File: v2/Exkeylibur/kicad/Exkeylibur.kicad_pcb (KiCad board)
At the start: 2 copper layers, 131.1 x 95.8 mm, 25 parts, among them SW1 SW_Push, SW10 SW_Push, SW11 SW_Push, SW12 SW_Push, SW13 SW_Push, SW14 SW_Push, SW15 SW_Push, SW16 SW_Push, SW17 SW_Push, SW18 SW_Push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

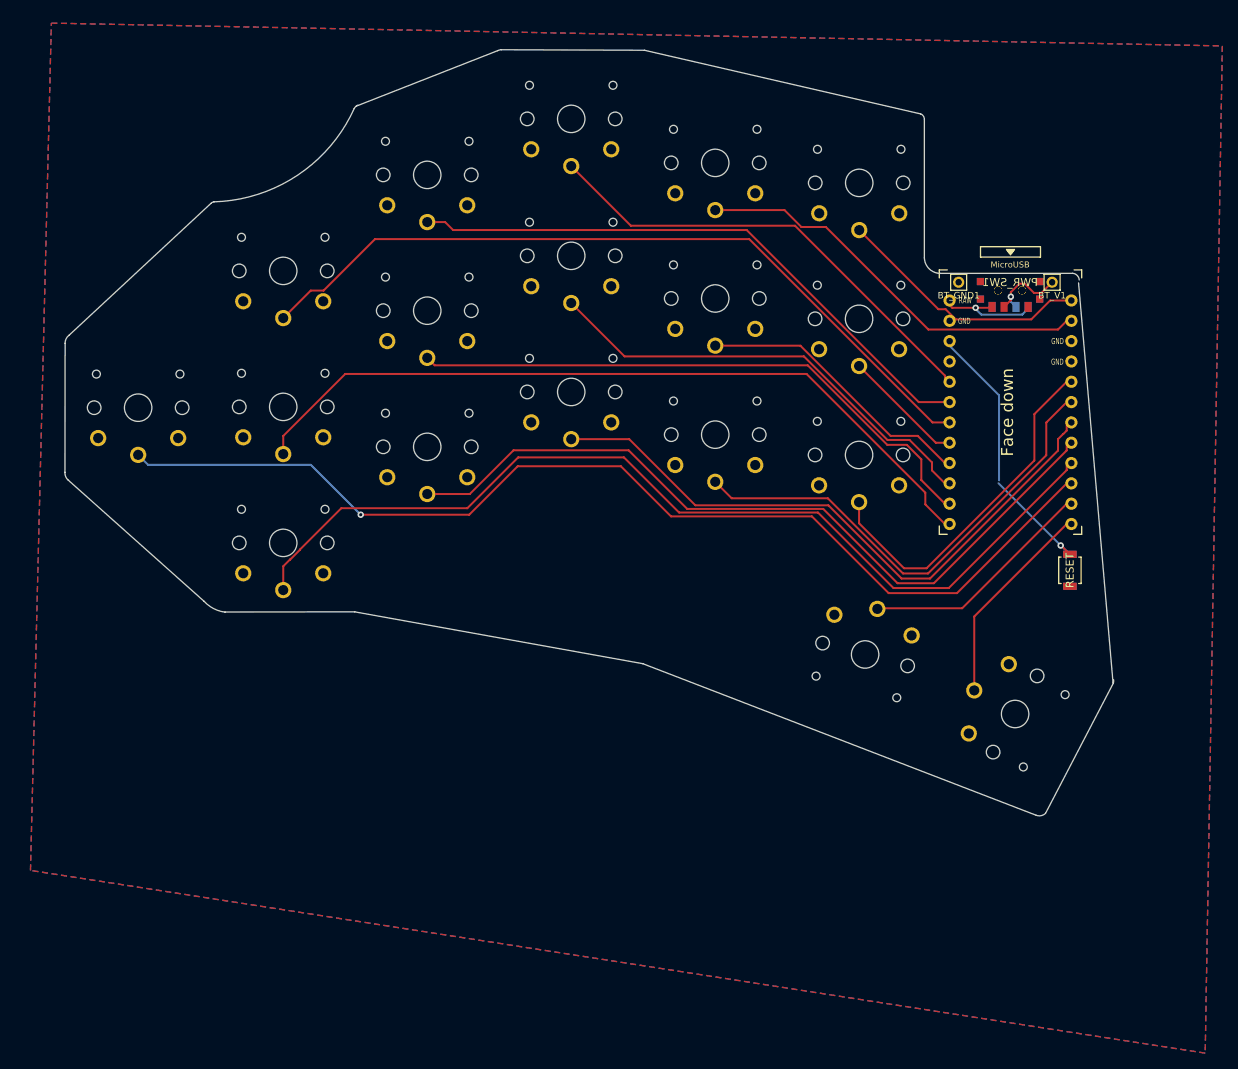
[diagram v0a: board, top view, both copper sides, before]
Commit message: add more room for the 1.5u keycap
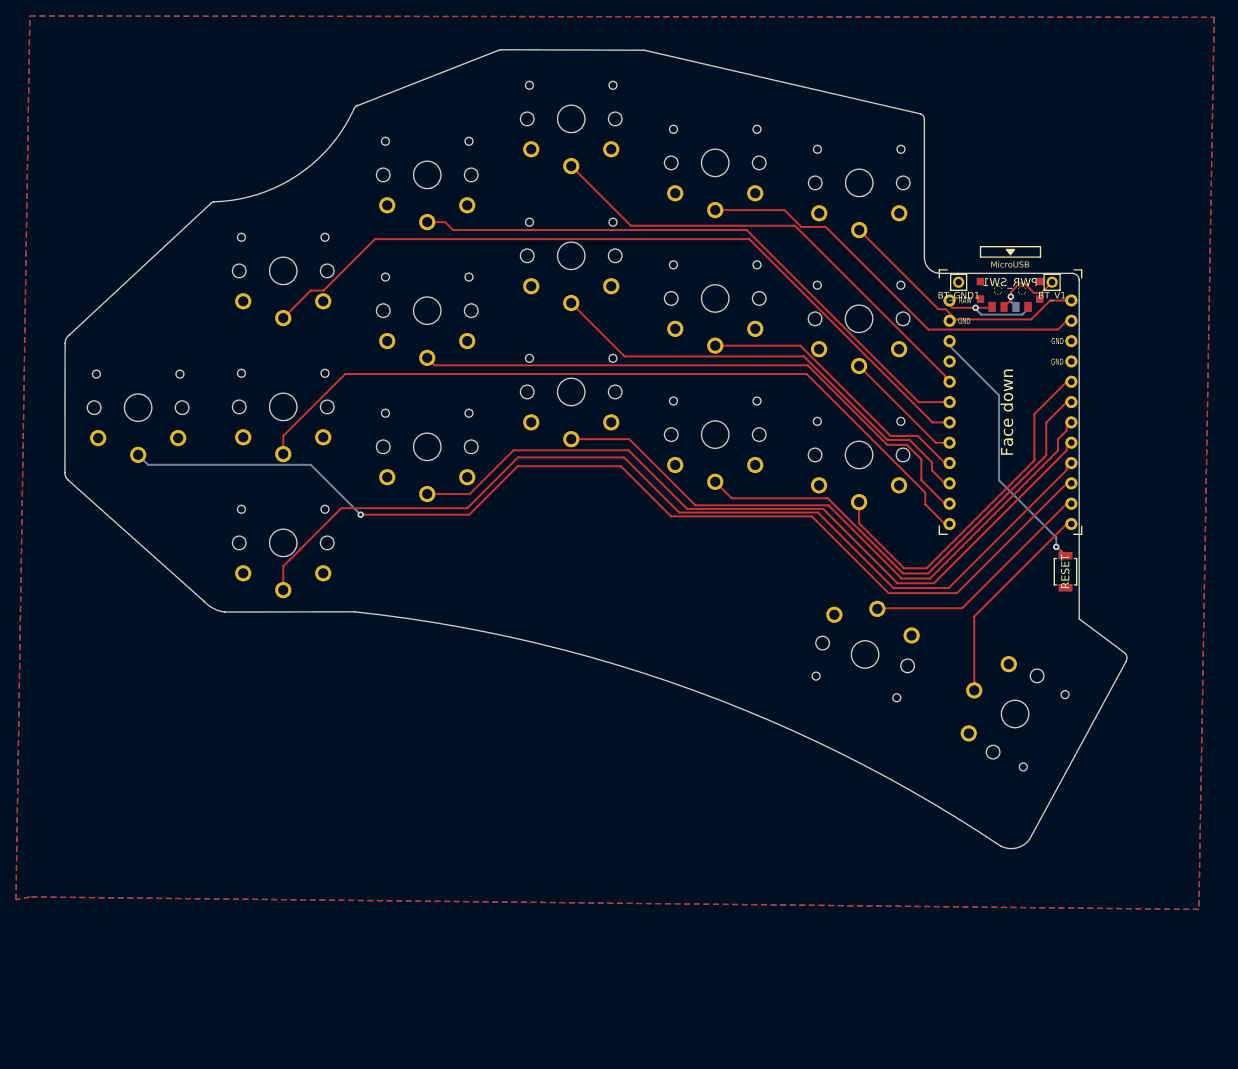
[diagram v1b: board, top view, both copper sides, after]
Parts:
- moved RSW1 0.58 mm to (145.6, 86.6) (x2)
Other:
- board size 131.1 x 95.8 mm -> 132.8 x 99.9 mm
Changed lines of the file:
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@@
   )
   (footprint "Exkeylibur:reset_switch" (layer "F.Cu")
-    (at 146.130425 86.446425 -90)
+    (at 145.57885 86.619158 -90)
     (descr "Ultra-small-sized Tactile Switch with High Contact Reliability, Top-actuated Model, without Ground Terminal, without Boss")
     (tags "Tactile Switch")
@@
   )
   (footprint "Exkeylibur:reset_switch" (layer "B.Cu")
-    (at 146.132 86.453692 -90)
+    (at 145.580425 86.626425 -90)
     (descr "Ultra-small-sized Tactile Switch with High Contact Reliability, Top-actuated Model, without Ground Terminal, without Boss")
     (tags "Tactile Switch")
@@
   (gr_arc (start 127.471526 29.394101) (mid 127.809899 29.662221) (end 127.93758 30.074631) (layer "Edge.Cuts") (width 0.05))
   (gr_line (start 129.972537 49.330129) (end 146.48327 49.322) (layer "Edge.Cuts") (width 0.05))
-  (gr_line (start 147.210425 50.516425) (end 151.520425 100.506425) (layer "Edge.Cuts") (width 0.05))
+  (gr_line (start 147.290425 50.156425) (end 147.290425 92.516425) (layer "Edge.Cuts") (width 0.05))
   (gr_line (start 38.740425 40.596425) (end 21.010425 57.076425) (layer "Edge.Cuts") (width 0.05))
   (gr_line (start 40.520425 91.656425) (end 56.730425 91.636425) (layer "Edge.Cuts") (width 0.05))
+  (gr_arc (start 56.730425 91.636425) (mid 98.901564 101.378791) (end 137.510425 120.936425) (layer "Edge.Cuts") (width 0.05))
   (gr_line (start 56.930425 28.421373) (end 74.610425 21.486425) (layer "Edge.Cuts") (width 0.05))
   (gr_arc (start 74.610425 21.486425) (mid 74.824112 21.406173) (end 75.050425 21.376425) (layer "Edge.Cuts") (width 0.05))
-  (gr_arc (start 151.600425 100.146425) (mid 151.595525 100.347935) (end 151.560425 100.546425) (layer "Edge.Cuts") (width 0.05))
+  (gr_arc (start 152.950425 96.746425) (mid 153.241962 97.238747) (end 153.170425 97.806425) (layer "Edge.Cuts") (width 0.05))
   (gr_arc (start 38.750425 40.586425) (mid 38.931438 40.448452) (end 39.150425 40.386425) (layer "Edge.Cuts") (width 0.05))
   (gr_arc (start 56.670425 28.716425) (mid 56.85267 28.482993) (end 57.090425 28.306425) (layer "Edge.Cuts") (width 0.05))
   (gr_arc (start 20.530425 58.076425) (mid 20.651266 57.519229) (end 21.010425 57.076425) (layer "Edge.Cuts") (width 0.05))
-  (gr_line (start 143.080425 116.826425) (end 151.560425 100.546425) (layer "Edge.Cuts") (width 0.05))
-  (gr_line (start 56.730425 91.636425) (end 92.740425 98.116425) (layer "Edge.Cuts") (width 0.05))
-  (gr_line (start 92.740425 98.116425) (end 141.920425 117.066425) (layer "Edge.Cuts") (width 0.05))
+  (gr_line (start 152.945425 96.741425) (end 147.290425 92.516425) (layer "Edge.Cuts") (width 0.05))
+  (gr_line (start 141.080425 120.086425) (end 153.170425 97.806425) (layer "Edge.Cuts") (width 0.05))
   (gr_line (start 75.050425 21.376425) (end 92.940425 21.436425) (layer "Edge.Cuts") (width 0.05))
   (gr_arc (start 56.670425 28.716425) (mid 49.583155 37.06267) (end 39.150425 40.386425) (layer "Edge.Cuts") (width 0.05))
-  (gr_arc (start 143.080425 116.826425) (mid 142.534749 117.112323) (end 141.920425 117.066425) (layer "Edge.Cuts") (width 0.05))
+  (gr_arc (start 141.080425 120.086425) (mid 139.45877 121.151864) (end 137.530425 120.936425) (layer "Edge.Cuts") (width 0.05))
   (gr_line (start 20.530425 58.076425) (end 20.510425 74.196425) (layer "Edge.Cuts") (width 0.05))
   (gr_line (start 92.940425 21.436425) (end 127.471526 29.394101) (layer "Edge.Cuts") (width 0.05))
@@
   (segment (start 138.740425 52.246425) (end 138.740425 52.864267) (width 0.25) (layer "B.Cu") (net 1))
   (segment (start 138.740425 52.864267) (end 139.397158 53.521) (width 0.25) (layer "B.Cu") (net 1))
-  (segment (start 144.975425 83.341425) (end 145.025425 83.341425) (width 0.25) (layer "F.Cu") (net 2))
-  (segment (start 145.025425 83.341425) (end 146.130425 84.446425) (width 0.25) (layer "F.Cu") (net 2))
-  (via (at 144.975425 83.341425) (size 0.8) (drill 0.4) (layers "F.Cu" "B.Cu") (net 2))
-  (segment (start 145.019733 83.341425) (end 146.132 84.453692) (width 0.25) (layer "B.Cu") (net 2))
-  (segment (start 144.975425 83.341425) (end 145.019733 83.341425) (width 0.25) (layer "B.Cu") (net 2))
+  (segment (start 144.42385 83.514158) (end 144.47385 83.514158) (width 0.25) (layer "F.Cu") (net 2))
+  (segment (start 144.47385 83.514158) (end 145.57885 84.619158) (width 0.25) (layer "F.Cu") (net 2))
+  (via (at 144.42385 83.514158) (size 0.8) (drill 0.4) (layers "F.Cu" "B.Cu") (net 2))
+  (segment (start 144.468158 83.514158) (end 145.580425 84.626425) (width 0.25) (layer "B.Cu") (net 2))
+  (segment (start 144.42385 82.34985) (end 144.42385 83.514158) (width 0.25) (layer "B.Cu") (net 2))
   (segment (start 130.508935 57.801212) (end 137.270425 64.562702) (width 0.25) (layer "B.Cu") (net 2))
   (segment (start 137.270425 64.562702) (end 137.270425 75.196425) (width 0.25) (layer "B.Cu") (net 2))
-  (segment (start 137.190425 75.556425) (end 144.975425 83.341425) (width 0.25) (layer "B.Cu") (net 2))
-  (segment (start 145.887692 84.453692) (end 146.132 84.453692) (width 0.25) (layer "B.Cu") (net 2))
+  (segment (start 137.270425 75.196425) (end 144.42385 82.34985) (width 0.25) (layer "B.Cu") (net 2))
+  (segment (start 145.336117 84.626425) (end 145.580425 84.626425) (width 0.25) (layer "B.Cu") (net 2))
   (segment (start 134.170875 92.219272) (end 134.170875 101.456425) (width 0.25) (layer "F.Cu") (net 4))
   (segment (start 145.728935 80.661212) (end 134.170875 92.219272) (width 0.25) (layer "F.Cu") (net 4))
@@
     (polygon
       (pts
-        (xy 165.180425 20.896425)
-        (xy 163.040425 146.796425)
-        (xy 16.200425 123.956425)
-        (xy 18.810425 18.046425)
+        (xy 164.160425 17.326425)
+        (xy 162.250425 128.836425)
+        (xy 16.120425 127.276425)
+        (xy 14.390425 127.616425)
+        (xy 16.120425 17.156425)
       )
     )
